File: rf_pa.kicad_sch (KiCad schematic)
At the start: 52 parts, among them Q1 BSS138, Q2 BSS138, Q3 NP100P04PDG, U1 LT1013DIDR, U2 LM317_SOT-223, U3 TL431, U4 RA60H3847H1

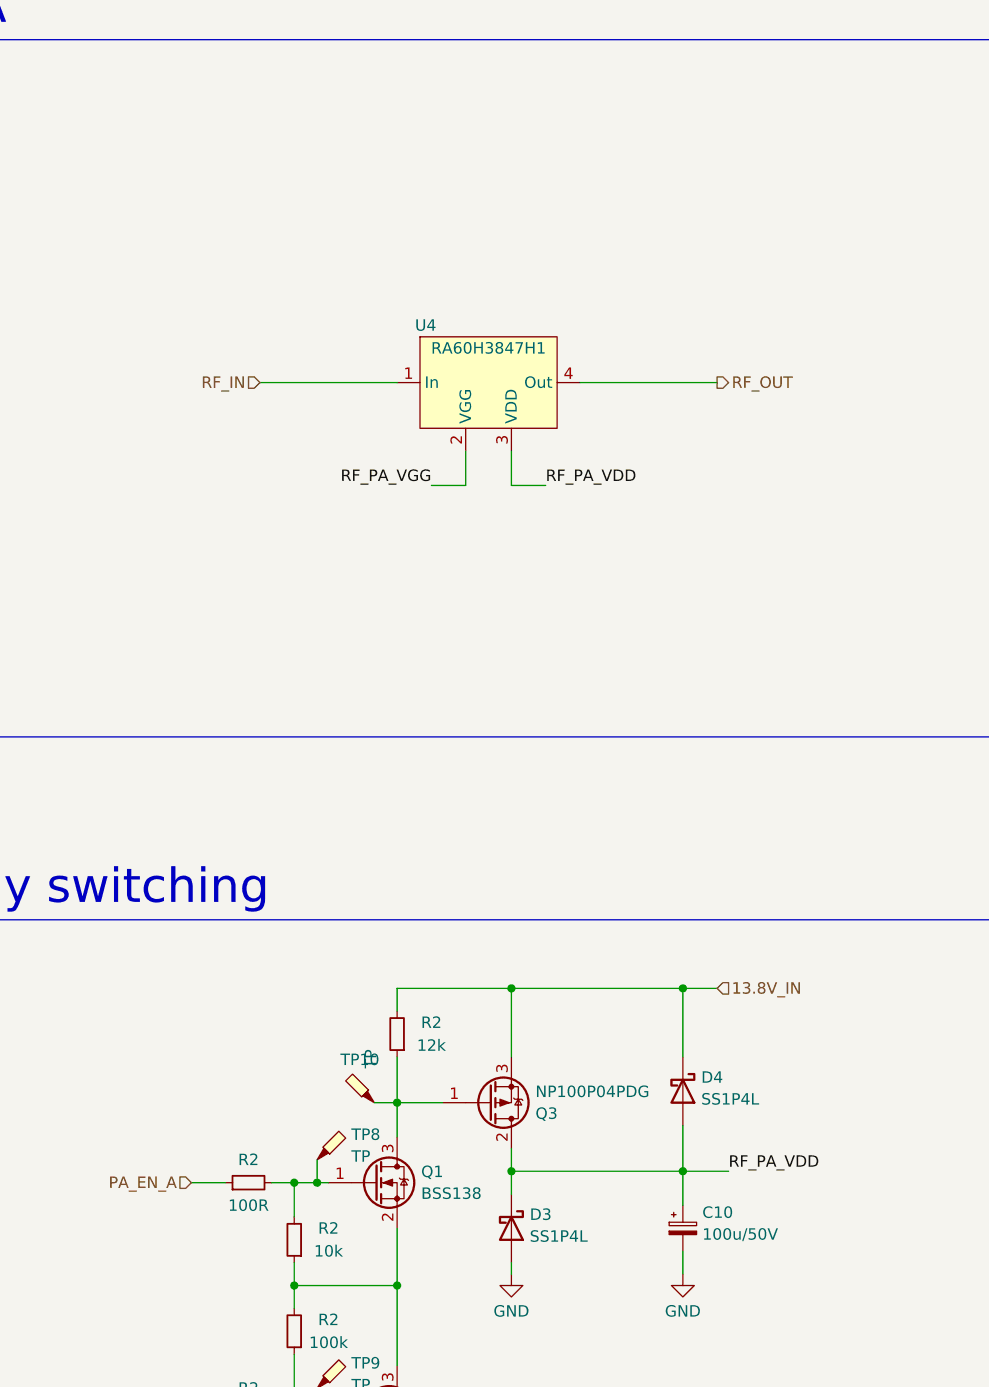
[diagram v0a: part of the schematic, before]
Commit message: TP updates, temp sensor added
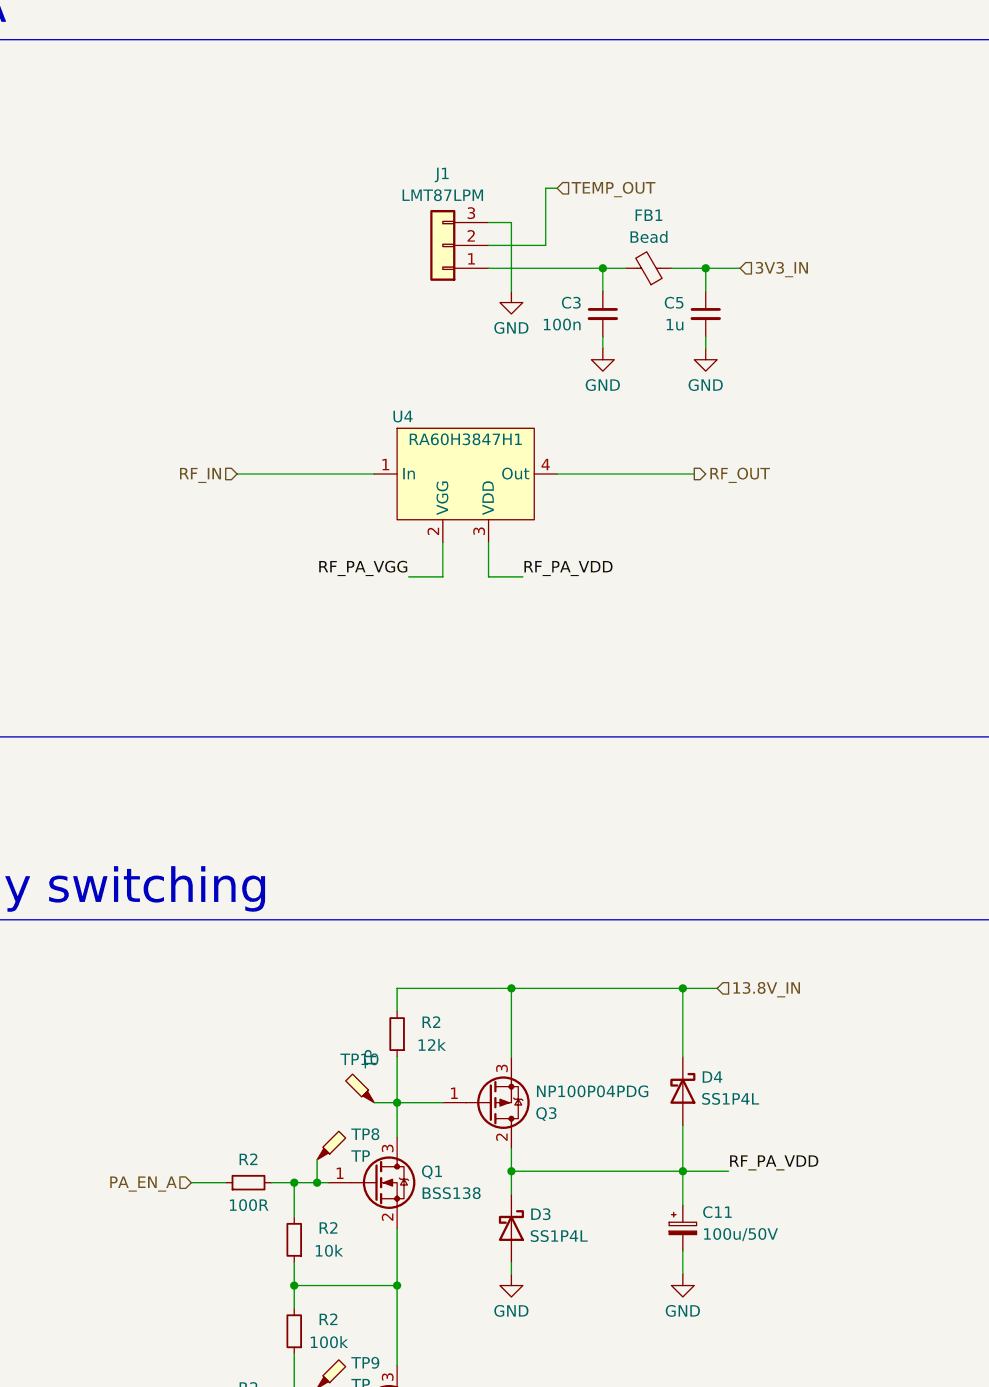
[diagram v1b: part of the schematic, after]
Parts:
- added C3: 100n, Capacitor_SMD:C_0603_1608Metric, symbol Device:C_Small
- added C5: 1u, Capacitor_SMD:C_0603_1608Metric, symbol Device:C_Small
- added FB1: Bead, Inductor_SMD:L_0603_1608Metric, symbol Device:FerriteBead_Small
- added J1: LMT87LPM, Connector_PinHeader_2.54mm:PinHeader_1x03_P2.54mm_Vertical_SMD_Pin1Left, symbol Connector_Generic:Conn_01x03
- renumbered C10 to C11
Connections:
- net GND: now also C3.2, C5.2, J1.3 (Pin_3)
- new net: C3.1, FB1.2, J1.1 (Pin_1)
- new net 3V3_IN: C5.1, FB1.1
- new net TEMP_OUT: J1.2 (Pin_2)
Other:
- moved on the sheet: U4

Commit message: date update
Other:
- title: M17 Remote Radio Unit - RF board -> Remote Radio Unit - RF board
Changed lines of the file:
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@@
   (paper "A3")
   (title_block
-    (title "M17 Remote Radio Unit - RF board")
-    (date "28-10-2023")
+    (title "Remote Radio Unit - RF board")
+    (date "30-10-2023")
     (rev "A")
     (company "M17 Project")

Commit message: MPN/PN update
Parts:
- C11: MPN (none) -> 50SEV100M8X10.5
- C3, C5: MPN (none) -> C0603C104M5RAC7411
- C3: MPN (none) -> GCM1885C1H392JA16J
- C4: MPN (none) -> C0603C102J5GAC7411
- C5: MPN (none) -> CL10B105KB8NQNC
- D1, D2: MPN (none) -> B160-13-F
- D3, D4: MPN (none) -> SS1P4LHM3/84A
- FB1: MPN (none) -> BLM18KG601SH1D
- J1: MPN (none) -> TSM-103-01-T-SV-TR
- Q1, Q2: MPN (none) -> BSS138P,215
- Q3: MPN (none) -> NP100P04PDG-E1-AY
- R2: MPN (none) -> CRCW06032K20FKEAC; PN (none) -> CRCW06032K20FKEAC
- R2: MPN (none) -> CRCW0603100KFKEAC; PN (none) -> CRCW0603100KFKEAC
- R2: MPN (none) -> RT0603FRE0710KL; PN (none) -> RT0603FRE0710KL
- R2: MPN (none) -> RK73H1JTTD7501F; PN (none) -> RK73H1JTTD7501F
- R2: MPN (none) -> CRGCQ0603J22K; PN (none) -> CRGCQ0603J22K
- R2: MPN (none) -> CRCW0603100RFKECC; PN (none) -> CRCW0603100RFKECC
- R2: MPN (none) -> WR06X2400FTL; PN (none) -> WR06X2400FTL
- R2: MPN (none) -> CRCW060312K0FKEAC; PN (none) -> CRCW060312K0FKEAC
- R2: MPN (none) -> RK73B1JRTTD472J; PN (none) -> RK73B1JRTTD472J
- R2: MPN (none) -> RC0603FR-071KL; PN (none) -> RC0603FR-071KL
- TP1, TP10, TP2, TP3, TP4, TP5, TP6, TP7, TP8, TP9, U4: MPN (none) -> -
- U1: MPN (none) -> LT1013DIDR
- U2: MPN (none) -> LM317MDCYRG3
- U3: MPN (none) -> TL431LIBIDBZR

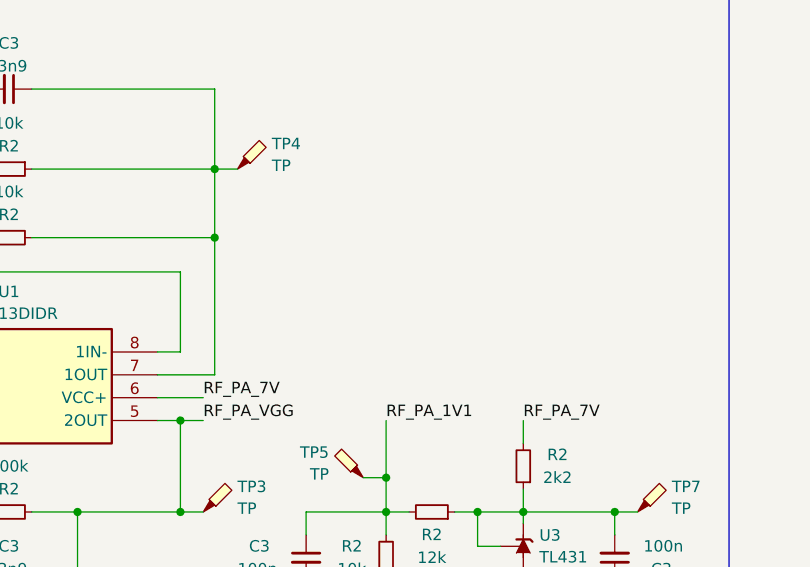
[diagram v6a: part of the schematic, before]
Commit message: diode polarization bugfix
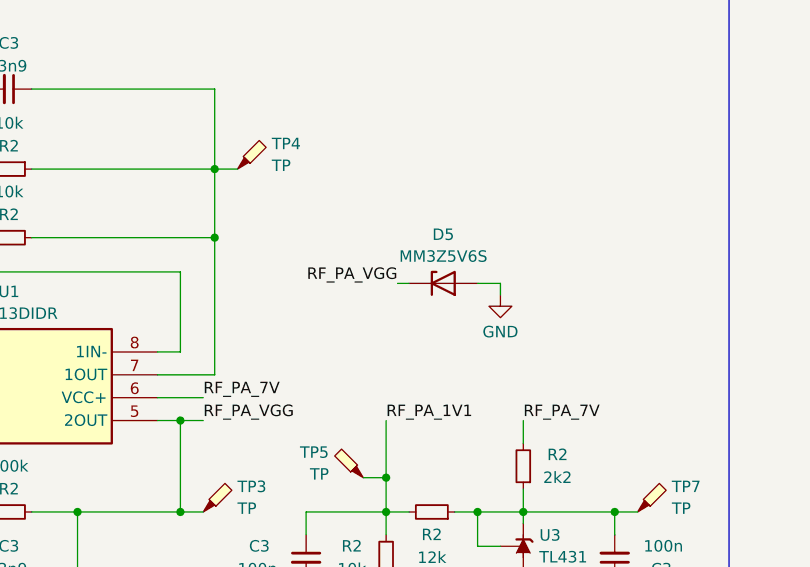
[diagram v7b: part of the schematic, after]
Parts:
- added D5: MM3Z5V6S, Diode_SMD:D_SOD-323, symbol Device:D_Zener
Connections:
- net GND: now also D5.2 (A)
- net RF_PA_VGG: now also D5.1 (K)
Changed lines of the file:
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@@
   (title_block
     (title "Remote Radio Unit - RF board")
-    (date "31-10-2023")
+    (date "03-11-2023")
     (rev "A")
     (company "M17 Project")
@@
     (stroke (width 0) (type default))
   )
+  (wire (pts (xy 168.91 88.9) (xy 171.45 88.9))
+    (stroke (width 0) (type default))
+  )
   (wire (pts (xy 306.07 191.77) (xy 306.07 194.31))
     (stroke (width 0) (type default))
@@
     (stroke (width 0) (type default))
   )
+  (wire (pts (xy 160.02 88.9) (xy 161.29 88.9))
+    (stroke (width 0) (type default))
+  )
   (wire (pts (xy 274.32 189.23) (xy 274.32 195.58))
     (stroke (width 0) (type default))
@@
   )
   (wire (pts (xy 173.99 111.76) (xy 173.99 114.3))
+    (stroke (width 0) (type default))
+  )
+  (wire (pts (xy 171.45 88.9) (xy 171.45 90.17))
     (stroke (width 0) (type default))
   )
@@
   (label "RF_PA_7V" (at 173.99 104.14 0) (fields_autoplaced)
     (effects (font (size 1.27 1.27)) (justify left bottom))
+  )
+  (label "RF_PA_VGG" (at 160.02 88.9 180) (fields_autoplaced)
+    (effects (font (size 1.27 1.27)) (justify right bottom))
   )
   (label "RF_PA_1V1" (at 158.75 104.14 0) (fields_autoplaced)
@@
         (path "/4c42207c-9e6b-42da-ad38-da126b892014/7ebe248e-d508-4395-8ad3-4ea02a49e591"
           (reference "R2") (unit 1)
+        )
+      )
+    )
+  )
+  (symbol (lib_id "power:GND") (at 171.45 90.17 0) (unit 1)
+    (in_bom yes) (on_board yes) (dnp no) (fields_autoplaced)
+    (property "Reference" "#PWR0135" (at 171.45 96.52 0)
+      (effects (font (size 1.27 1.27)) hide)
+    )
+    (property "Value" "GND" (at 171.45 94.3031 0)
+      (effects (font (size 1.27 1.27)))
+    )
+    (property "Footprint" "" (at 171.45 90.17 0)
+      (effects (font (size 1.27 1.27)) hide)
+    )
+    (property "Datasheet" "" (at 171.45 90.17 0)
+      (effects (font (size 1.27 1.27)) hide)
+    )
+    (pin "1")
+    (instances
+      (project "m17-rru-rf"
+        (path "/4c42207c-9e6b-42da-ad38-da126b892014/7ebe248e-d508-4395-8ad3-4ea02a49e591"
+          (reference "#PWR0135") (unit 1)
         )
       )
@@
     )
   )
-  (symbol (lib_id "Device:D_Schottky") (at 306.07 173.99 270) (unit 1)
+  (symbol (lib_name "D_Schottky_1") (lib_id "Device:D_Schottky") (at 306.07 173.99 270) (unit 1)
     (in_bom yes) (on_board yes) (dnp no) (fields_autoplaced)
     (property "Reference" "D4" (at 308.102 172.4604 90)
@@
         )
       )
+    )
+  )
+  (symbol (lib_id "Device:D_Zener") (at 165.1 88.9 0) (unit 1)
+    (in_bom yes) (on_board yes) (dnp no) (fields_autoplaced)
+    (property "Reference" "D5" (at 165.1 83.4857 0)
+      (effects (font (size 1.27 1.27)))
+    )
+    (property "Value" "MM3Z5V6S" (at 165.1 85.9099 0)
+      (effects (font (size 1.27 1.27)))
+    )
+    (property "Footprint" "Diode_SMD:D_SOD-323" (at 165.1 88.9 0)
+      (effects (font (size 1.27 1.27)) hide)
+    )
+    (property "Datasheet" "~" (at 165.1 88.9 0)
+      (effects (font (size 1.27 1.27)) hide)
+    )
+    (property "PN" "MM3Z5V6ST1G" (at 165.1 88.9 0)
+      (effects (font (size 1.27 1.27)) hide)
+    )
+    (property "MPN" "MM3Z5V6ST1G" (at 165.1 88.9 0)
+      (effects (font (size 1.27 1.27)) hide)
+    )
+    (pin "1")
+    (pin "2")
+    (instances
+      (project "m17-rru-rf"
+        (path "/4c42207c-9e6b-42da-ad38-da126b892014/7ebe248e-d508-4395-8ad3-4ea02a49e591"
+          (reference "D5") (unit 1)
+        )
+      )
